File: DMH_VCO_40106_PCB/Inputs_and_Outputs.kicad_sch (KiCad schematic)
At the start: 11 parts, among them J1 TS_Jack_6.35mm_Sw, J2 TS_Jack_6.35mm_Sw, J3 TS_Jack_6.35mm_Sw, J4 TS_Jack_6.35mm_Sw, J5 TS_Jack_6.35mm_Sw, J6 TS_Jack_6.35mm_Sw, J7 TS_Jack_6.35mm_Sw, J8 TS_Jack_6.35mm_Sw, J9 TS_Jack_6.35mm_Sw, SW1 SW_SPDT, SW2 SW_SPDT

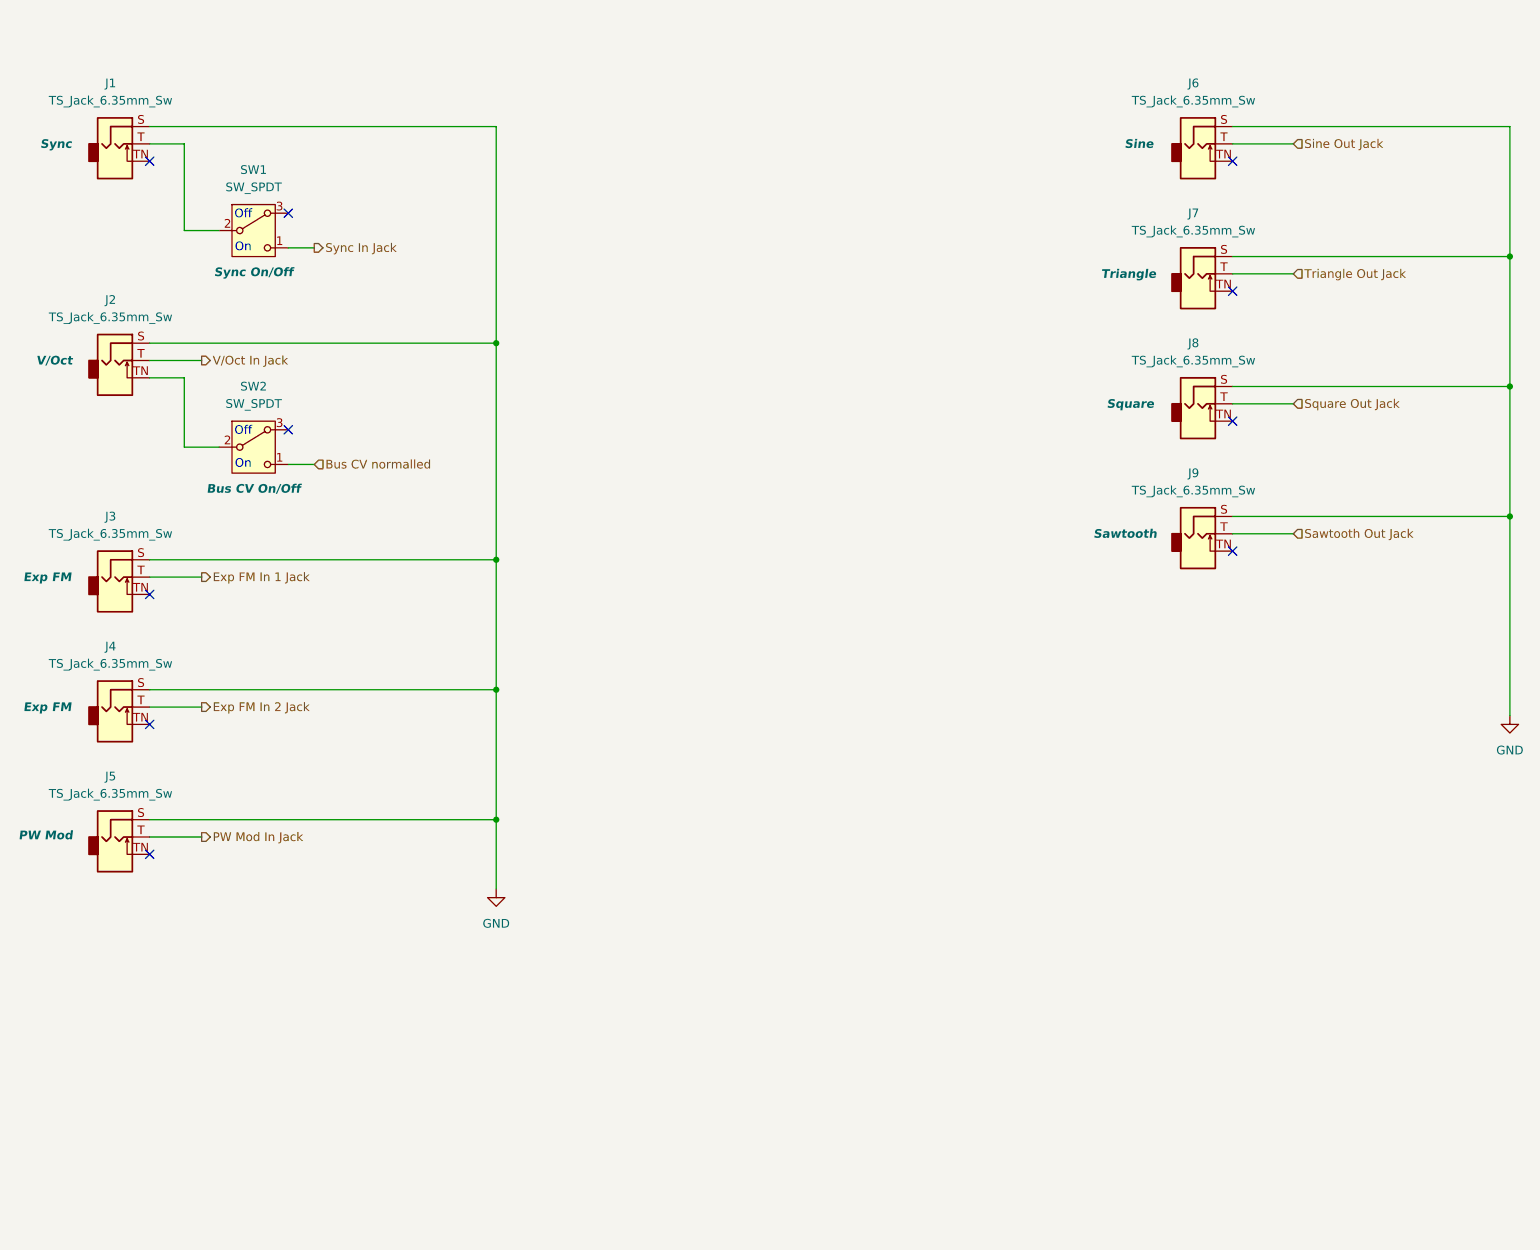
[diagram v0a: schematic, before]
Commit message: Added normalled backbone connections
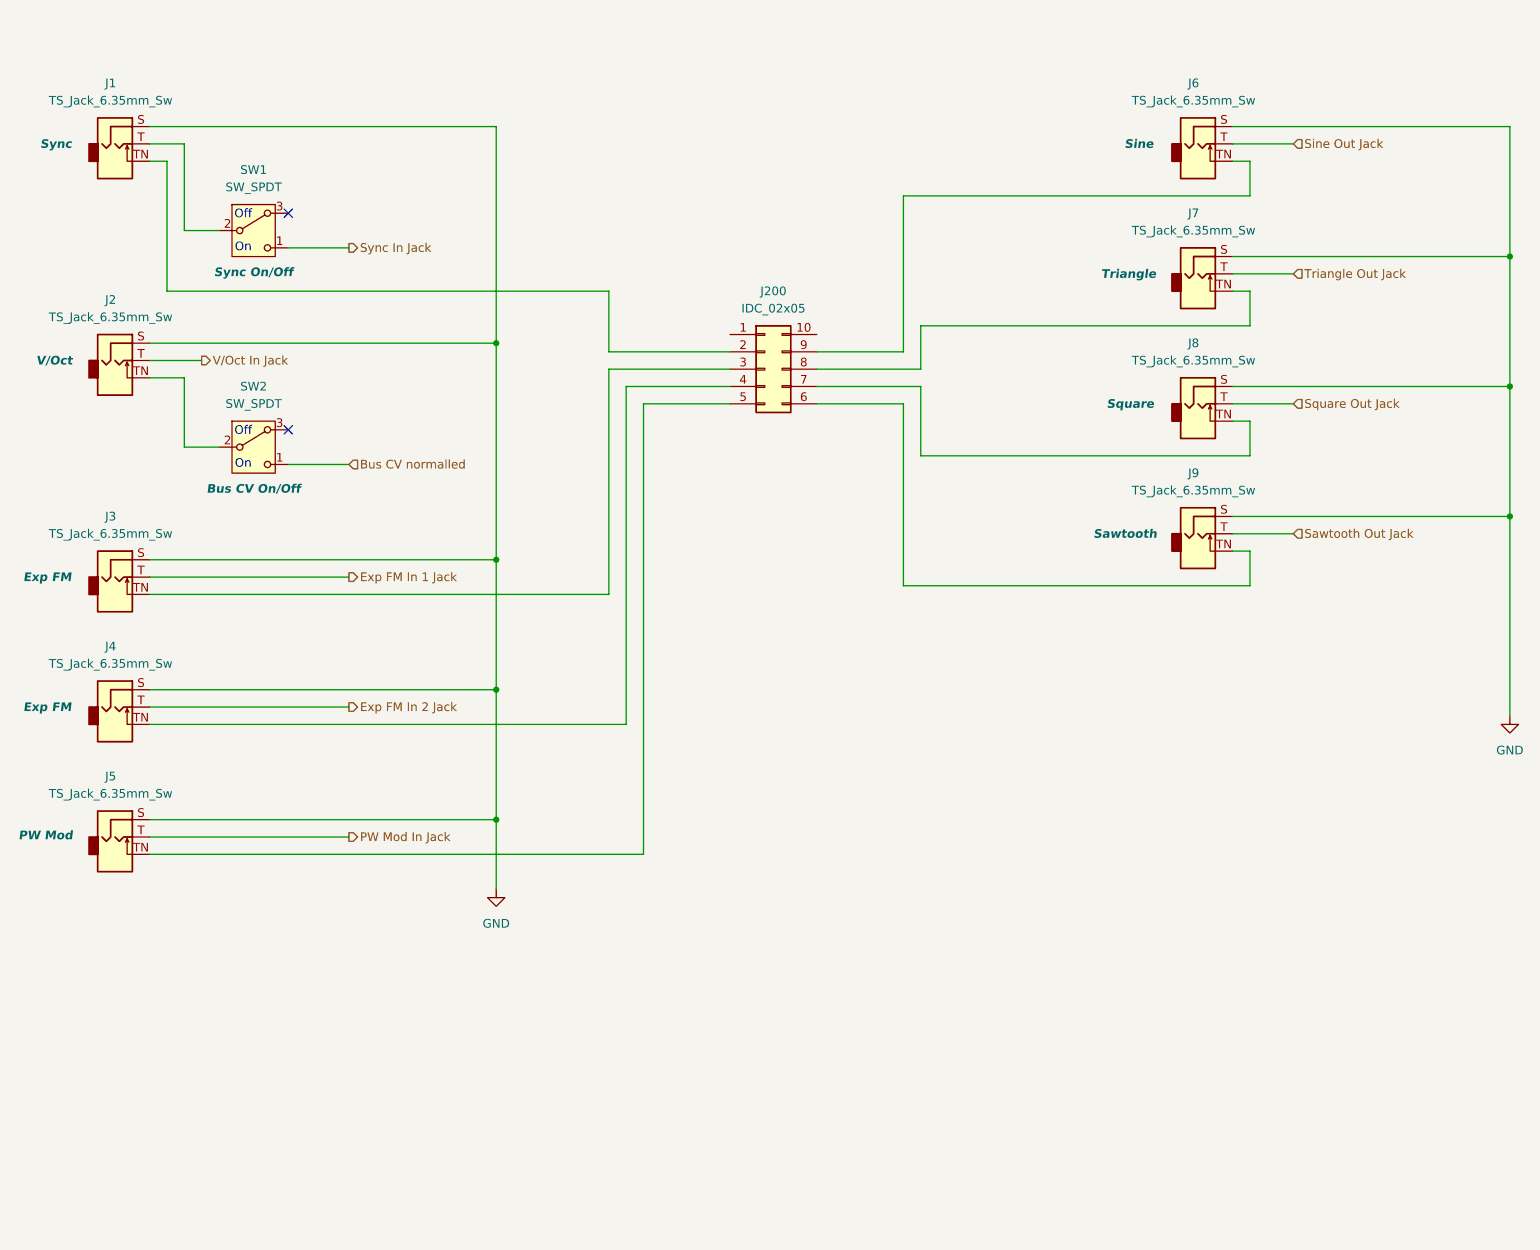
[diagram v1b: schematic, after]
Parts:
- added J200: IDC_02x05, SynthStuff:IDC-Header_2x05_P2.54mm_Vertical_BackBone, symbol SynthStuff:BackBone_Connector_10Pin
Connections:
- net at J1.TN: now also J200.2 (Pin_2)
- net at J3.TN: now also J200.3 (Pin_3)
- net at J4.TN: now also J200.4 (Pin_4)
- net at J5.TN: now also J200.5 (Pin_5)
- net at J9.TN: now also J200.6 (Pin_6)
- net at J7.TN: now also J200.8 (Pin_8)
- net at J8.TN: now also J200.7 (Pin_7)
- net at J6.TN: now also J200.9 (Pin_9)
- no-connect marks 10 -> 2

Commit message: Prepared Inputs/Outputs sheet to split in 2 PCBs
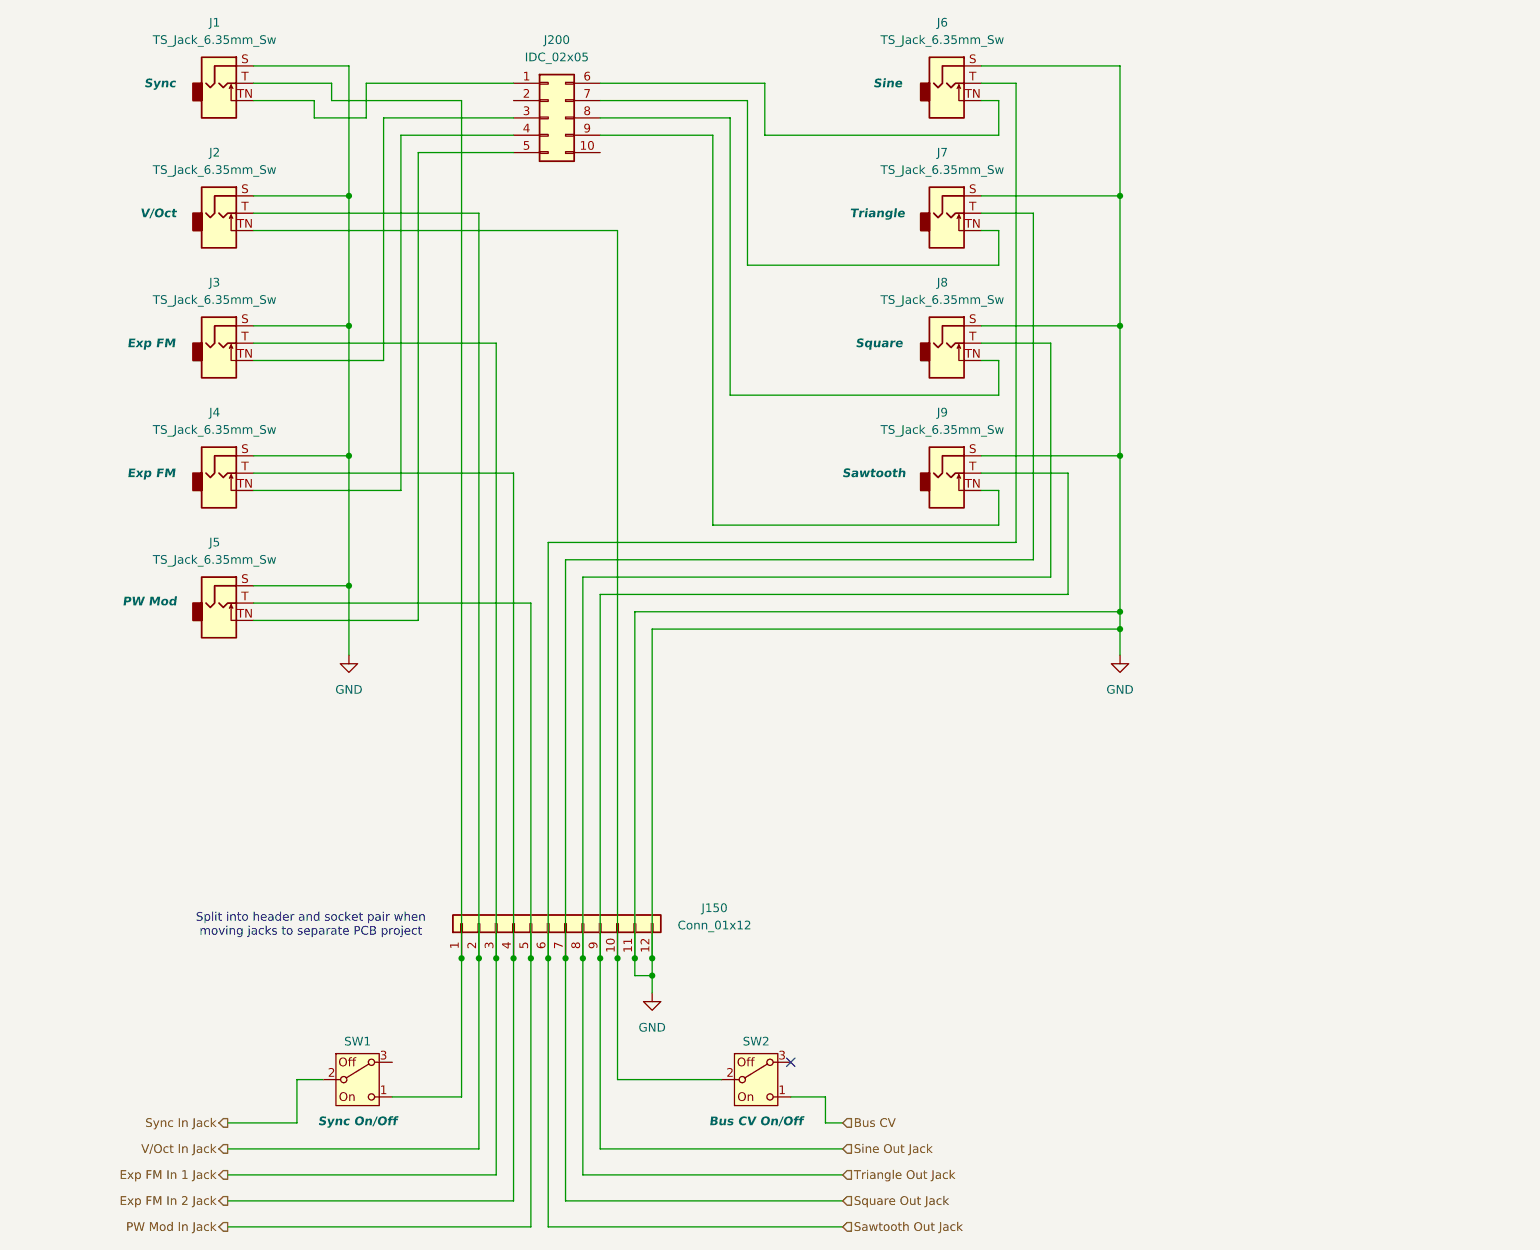
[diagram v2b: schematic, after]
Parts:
- removed SW1: SW_SPDT, symbol Switch:SW_SPDT_321
- added J150: Conn_01x12, Connector_PinHeader_2.54mm:PinHeader_1x12_P2.54mm_Vertical, symbol Connector_Generic:Conn_01x12
- added SW1: SW_SPDT_321_OnOff, symbol SynthStuff:SW_SPDT_321_OnOff
- SW2: value SW_SPDT -> SW_SPDT_321_OnOff; symbol Switch:SW_SPDT_321 -> SynthStuff:SW_SPDT_321_OnOff
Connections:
- net Exp FM In 1 Jack: now also J150.3 (Pin_3)
- net Exp FM In 2 Jack: now also J150.4 (Pin_4)
- net GND: now also J150.11 (Pin_11), J150.12 (Pin_12)
- net PW Mod In Jack: now also J150.5 (Pin_5)
- net Sawtooth Out Jack: now also J6.T, J150.6 (Pin_6); no longer J9.T
- net Sine Out Jack: now also J9.T, J150.9 (Pin_9); no longer J6.T
- net Square Out Jack: now also J7.T, J150.7 (Pin_7); no longer J8.T
- net Sync In Jack: now also SW1.2 (B)
- net Triangle Out Jack: now also J8.T, J150.8 (Pin_8); no longer J7.T
- net V/Oct In Jack: now also J150.2 (Pin_2)
- net at J1.T: now also J150.1 (Pin_1), SW1.1 (C)
- net at J1.TN: now also J200.1 (Pin_1); no longer J200.2 (Pin_2)
- net at J2.TN, SW2.2 (B): now also J150.10 (Pin_10)
- net at J200.6 (Pin_6): now also J6.TN; no longer J9.TN
- net at J200.7 (Pin_7): now also J7.TN; no longer J8.TN
- net at J200.8 (Pin_8): now also J8.TN; no longer J7.TN
- net at J200.9 (Pin_9): now also J9.TN; no longer J6.TN
- net Bus CV normalled renamed Bus CV
- no-connect marks 2 -> 1
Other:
- note added: "Split into header and socket pair when moving jacks to separate PCB project"
- note removed: "Off"
- note removed: "On"
- moved on the sheet: J1, J2, J200, J3, J4, J5, J6, J7, J8, J9

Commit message: Started main PCB design
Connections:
- no-connect marks 1 -> 4
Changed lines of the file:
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@@
+	)
+	(no_connect
+		(at 90.17 168.91)
 	)
 	(no_connect
 		(at 148.59 168.91)
 	)
+	(no_connect
+		(at 107.95 27.94)
+	)
+	(no_connect
+		(at 120.65 35.56)
+	)
 	(wire
